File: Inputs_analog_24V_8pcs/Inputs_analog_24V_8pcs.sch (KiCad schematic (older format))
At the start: 14 parts, among them J1 Screw_Terminal_01x02, J2 Screw_Terminal_01x02, J3 Screw_Terminal_01x06, U1 SN74HC14N, U2 SN74HC14N, U3 74HC151N.652

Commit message: Update pcb
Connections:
- net GND: no longer U1.10 (5Y), U1.11 (5A), U1.12 (6Y), U1.13 (6A), U2.10 (5Y), U2.11 (5A), U2.12 (6Y), U2.13 (6A)
- net input_1: no longer U1.1 (1A)
- net input_2: no longer U1.3 (2A)
- net input_3: no longer U1.5 (3A)
- net input_4: no longer U1.9 (4A)
- net input_5: no longer U2.1 (1A)
- net input_6: no longer U2.3 (2A)
- net input_7: no longer U2.5 (3A)
- net input_8: no longer U2.9 (4A)
- net at U1.2 (1Y): no longer U3.4 (I0)
- net at U1.4 (2Y): no longer U3.3 (I1)
- net at U1.6 (3Y): no longer U3.2 (I2)
- net at U1.8 (4Y): no longer U3.1 (I3)
- net at U2.2 (1Y): no longer U3.15 (I4)
- net at U2.4 (2Y): no longer U3.14 (I5)
- net at U2.6 (3Y): no longer U3.13 (I6)
- net at U2.8 (4Y): no longer U3.12 (I7)
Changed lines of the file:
@@
 F1 "Inputs.sch" 50
 $EndSheet
-Text GLabel 1500 3900 0    50   Input ~ 0
+Text GLabel 1500 3400 0    50   Input ~ 0
 input_1
-Text GLabel 1500 3800 0    50   Input ~ 0
+Text GLabel 1500 3500 0    50   Input ~ 0
 input_2
-Text GLabel 1500 3700 0    50   Input ~ 0
+Text GLabel 1500 3600 0    50   Input ~ 0
 input_3
-Text GLabel 1500 3600 0    50   Input ~ 0
+Text GLabel 1500 3950 0    50   Input ~ 0
 input_4
+Text GLabel 1500 4750 0    50   Input ~ 0
+input_5
+Text GLabel 1500 5200 0    50   Input ~ 0
+input_6
 Text GLabel 1500 5400 0    50   Input ~ 0
-input_5
+input_7
 Text GLabel 1500 5300 0    50   Input ~ 0
-input_6
-Wire Wire Line
-	1500 3600 1950 3600
-Wire Wire Line
-	1500 3700 1950 3700
-Wire Wire Line
-	1500 3800 1950 3800
-Wire Wire Line
-	1500 3900 1950 3900
-Text GLabel 1500 5200 0    50   Input ~ 0
-input_7
-Text GLabel 1500 5100 0    50   Input ~ 0
 input_8
-Wire Wire Line
-	1500 5300 1950 5300
-Wire Wire Line
-	1500 5400 1950 5400
 $Comp
 L power:GND #PWR04
@@
 	1    0    0    -1
 $EndComp
-Wire Wire Line
-	1900 4900 1950 4900
-Wire Wire Line
-	1950 5000 1900 5000
-Connection ~ 1900 5000
-Wire Wire Line
-	1900 5000 1900 4900
 $Comp
 L power:+5V #PWR09
@@
 Wire Wire Line
 	2700 5500 2700 5700
-Connection ~ 2700 5500
-Wire Wire Line
-	2650 5000 2700 5000
-Wire Wire Line
-	2650 4900 2700 4900
-Wire Wire Line
-	2700 4900 2700 5000
-Connection ~ 2700 5000
 $Comp
 L power:+5V #PWR011
@@
 Wire Wire Line
 	4550 3900 4550 4050
-Wire Wire Line
-	1900 5000 1900 5700
-Wire Wire Line
-	1500 5200 1950 5200
-Wire Wire Line
-	1500 5100 1950 5100
 $Comp
 L power:GND #PWR03
@@
 $EndComp
 Wire Wire Line
-	1950 3500 1900 3500
-Wire Wire Line
-	1900 3500 1900 4050
-Wire Wire Line
-	1950 3400 1900 3400
-Wire Wire Line
-	1900 3400 1900 3500
-Connection ~ 1900 3500
-Wire Wire Line
-	2650 3500 2700 3500
-Wire Wire Line
-	2700 3500 2700 4000
-Connection ~ 2700 4000
-Wire Wire Line
-	2650 3400 2700 3400
-Wire Wire Line
-	2700 3400 2700 3500
-Connection ~ 2700 3500
-Wire Wire Line
-	3750 5400 3750 3500
-Wire Wire Line
-	3750 3500 3800 3500
-Wire Wire Line
-	3650 5300 3650 3400
-Wire Wire Line
-	3650 3400 3800 3400
-Wire Wire Line
-	3800 3300 3550 3300
-Wire Wire Line
-	3550 3300 3550 5200
-Wire Wire Line
-	3450 5100 3450 3200
-Wire Wire Line
-	3450 3200 3800 3200
-Wire Wire Line
-	2650 5100 3450 5100
-Wire Wire Line
-	2650 5200 3550 5200
-Wire Wire Line
-	2650 5300 3650 5300
-Wire Wire Line
-	2700 5000 2700 5500
-Wire Wire Line
-	3750 5400 2650 5400
-Wire Wire Line
-	2650 3600 3800 3600
-Wire Wire Line
-	2650 3700 3800 3700
-Wire Wire Line
-	2650 3800 3800 3800
-Wire Wire Line
-	2650 3900 3800 3900
-Wire Wire Line
 	4500 3300 4750 3300

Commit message: Update pcb
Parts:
- added R52, R53: 0, Resistor_THT:R_Axial_DIN0207_L6.3mm_D2.5mm_P7.62mm_Horizontal, symbol Device:R
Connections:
- net GND: now also U2.10 (5Y), U2.11 (5A), U2.12 (6Y), U2.13 (6A), R52.1, R53.1; no longer U1.7 (GND)
- net input_1: now also U1.13 (6A)
- net input_2: now also U1.11 (5A)
- net input_3: now also U1.9 (4A)
- net input_4: now also U2.9 (4A)
- net input_5: now also U2.5 (3A)
- net input_6: now also U2.3 (2A)
- net input_7: now also U1.1 (1A)
- net input_8: now also U2.1 (1A)
- net at U1.10 (5Y): now also U3.15 (I4)
- net at U1.12 (6Y): now also U3.14 (I5)
- net at U1.2 (1Y): now also U3.4 (I0)
- net at U1.3 (2A): now also U1.4 (2Y), U1.5 (3A), U1.6 (3Y), R52.2
- net at U1.8 (4Y): now also U3.1 (I3)
- new net: R53.2, U1.7 (GND)
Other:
- moved on the sheet: C2, U2
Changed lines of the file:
@@
 L Inputs_library:SN74HC14N U2
 U 1 1 5EA6DB6E
-P 2550 5950
-F 0 "U2" H 2300 7367 50  0000 C CNN
-F 1 "SN74HC14N" H 2300 7276 50  0000 C CNN
-F 2 "Package_DIP:DIP-14_W7.62mm" H 2550 5950 50  0001 C CNN
-F 3 "" H 2550 5950 50  0001 C CNN
-	1    2550 5950
+P 2550 6350
+F 0 "U2" H 2300 7767 50  0000 C CNN
+F 1 "SN74HC14N" H 2300 7676 50  0000 C CNN
+F 2 "Package_DIP:DIP-14_W7.62mm" H 2550 6350 50  0001 C CNN
+F 3 "" H 2550 6350 50  0001 C CNN
+	1    2550 6350
 	1    0    0    -1
 $EndComp
@@
 $EndComp
 $Sheet
-S 1000 3100 750  2700
+S 1000 3100 650  3200
 U 5EB670BF
 F0 "Inputs" 50
@@
 Text GLabel 1500 3600 0    50   Input ~ 0
 input_3
-Text GLabel 1500 3950 0    50   Input ~ 0
+Text GLabel 1500 5500 0    50   Input ~ 0
 input_4
-Text GLabel 1500 4750 0    50   Input ~ 0
+Text GLabel 1500 5600 0    50   Input ~ 0
 input_5
-Text GLabel 1500 5200 0    50   Input ~ 0
+Text GLabel 1500 5700 0    50   Input ~ 0
 input_6
-Text GLabel 1500 5400 0    50   Input ~ 0
+Text GLabel 1500 3900 0    50   Input ~ 0
 input_7
-Text GLabel 1500 5300 0    50   Input ~ 0
+Text GLabel 1500 5800 0    50   Input ~ 0
 input_8
 $Comp
 L power:GND #PWR04
 U 1 1 5EB7A823
-P 1900 5700
-F 0 "#PWR04" H 1900 5450 50  0001 C CNN
-F 1 "GND" H 1905 5527 50  0000 C CNN
-F 2 "" H 1900 5700 50  0001 C CNN
-F 3 "" H 1900 5700 50  0001 C CNN
-	1    1900 5700
+P 1900 6100
+F 0 "#PWR04" H 1900 5850 50  0001 C CNN
+F 1 "GND" H 1905 5927 50  0000 C CNN
+F 2 "" H 1900 6100 50  0001 C CNN
+F 3 "" H 1900 6100 50  0001 C CNN
+	1    1900 6100
 	1    0    0    -1
 $EndComp
@@
 L power:GND #PWR06
 U 1 1 5EBDD6D8
-P 2700 5700
-F 0 "#PWR06" H 2700 5450 50  0001 C CNN
-F 1 "GND" H 2705 5527 50  0000 C CNN
-F 2 "" H 2700 5700 50  0001 C CNN
-F 3 "" H 2700 5700 50  0001 C CNN
-	1    2700 5700
-	1    0    0    -1
-$EndComp
-Wire Wire Line
-	2650 5500 2700 5500
-Wire Wire Line
-	2700 5500 2700 5700
+P 2700 6100
+F 0 "#PWR06" H 2700 5850 50  0001 C CNN
+F 1 "GND" H 2705 5927 50  0000 C CNN
+F 2 "" H 2700 6100 50  0001 C CNN
+F 3 "" H 2700 6100 50  0001 C CNN
+	1    2700 6100
+	1    0    0    -1
+$EndComp
+Wire Wire Line
+	2650 5900 2700 5900
+Wire Wire Line
+	2700 5900 2700 6100
 $Comp
 L power:+5V #PWR011
 U 1 1 5EBE4E40
-P 3050 4800
-F 0 "#PWR011" H 3050 4650 50  0001 C CNN
-F 1 "+5V" V 3065 4928 50  0000 L CNN
-F 2 "" H 3050 4800 50  0001 C CNN
-F 3 "" H 3050 4800 50  0001 C CNN
-	1    3050 4800
-	0    1    1    0
-$EndComp
-Wire Wire Line
-	2650 4800 2700 4800
+P 3050 5200
+F 0 "#PWR011" H 3050 5050 50  0001 C CNN
+F 1 "+5V" V 3065 5328 50  0000 L CNN
+F 2 "" H 3050 5200 50  0001 C CNN
+F 3 "" H 3050 5200 50  0001 C CNN
+	1    3050 5200
+	0    1    1    0
+$EndComp
+Wire Wire Line
+	2650 5200 2700 5200
 $Comp
 L Device:C C2
 U 1 1 5EBE4E47
-P 2900 4650
-F 0 "C2" V 2648 4650 50  0000 C CNN
-F 1 "0,47μF" V 2739 4650 50  0000 C CNN
-F 2 "Capacitor_THT:C_Disc_D4.3mm_W1.9mm_P5.00mm" H 2938 4500 50  0001 C CNN
-F 3 "~" H 2900 4650 50  0001 C CNN
-	1    2900 4650
-	0    1    1    0
-$EndComp
-Wire Wire Line
-	2750 4650 2700 4650
-Wire Wire Line
-	2700 4650 2700 4800
-Connection ~ 2700 4800
+P 2900 5050
+F 0 "C2" V 2648 5050 50  0000 C CNN
+F 1 "0,47μF" V 2739 5050 50  0000 C CNN
+F 2 "Capacitor_THT:C_Disc_D4.3mm_W1.9mm_P5.00mm" H 2938 4900 50  0001 C CNN
+F 3 "~" H 2900 5050 50  0001 C CNN
+	1    2900 5050
+	0    1    1    0
+$EndComp
+Wire Wire Line
+	2750 5050 2700 5050
+Wire Wire Line
+	2700 5050 2700 5200
+Connection ~ 2700 5200
 $Comp
 L power:GND #PWR010
 U 1 1 5EBE4E50
-P 3050 4650
-F 0 "#PWR010" H 3050 4400 50  0001 C CNN
-F 1 "GND" H 3055 4477 50  0000 C CNN
-F 2 "" H 3050 4650 50  0001 C CNN
-F 3 "" H 3050 4650 50  0001 C CNN
-	1    3050 4650
+P 3050 5050
+F 0 "#PWR010" H 3050 4800 50  0001 C CNN
+F 1 "GND" H 3055 4877 50  0000 C CNN
+F 2 "" H 3050 5050 50  0001 C CNN
+F 3 "" H 3050 5050 50  0001 C CNN
+	1    3050 5050
 	0    -1   -1   0
 $EndComp
 Wire Wire Line
-	2700 4800 3050 4800
-$Comp
-L power:GND #PWR05
-U 1 1 5EBE68A6
-P 2700 4050
-F 0 "#PWR05" H 2700 3800 50  0001 C CNN
-F 1 "GND" H 2705 3877 50  0000 C CNN
-F 2 "" H 2700 4050 50  0001 C CNN
-F 3 "" H 2700 4050 50  0001 C CNN
-	1    2700 4050
-	1    0    0    -1
-$EndComp
-Wire Wire Line
-	2650 4000 2700 4000
-Wire Wire Line
-	2700 4000 2700 4050
+	2700 5200 3050 5200
 $Comp
 L power:+5V #PWR015
@@
 L power:GND #PWR03
 U 1 1 5EC164A3
-P 1900 4050
-F 0 "#PWR03" H 1900 3800 50  0001 C CNN
-F 1 "GND" H 1905 3877 50  0000 C CNN
-F 2 "" H 1900 4050 50  0001 C CNN
-F 3 "" H 1900 4050 50  0001 C CNN
-	1    1900 4050
+P 1900 4500
+F 0 "#PWR03" H 1900 4250 50  0001 C CNN
+F 1 "GND" H 1905 4327 50  0000 C CNN
+F 2 "" H 1900 4500 50  0001 C CNN
+F 3 "" H 1900 4500 50  0001 C CNN
+	1    1900 4500
 	1    0    0    -1
 $EndComp
@@
 	1    0    0    -1
 $EndComp
+Wire Wire Line
+	1500 3400 1950 3400
+Wire Wire Line
+	1500 3500 1950 3500
+Wire Wire Line
+	1500 3600 1950 3600
+Wire Wire Line
+	2650 3400 3800 3400
+Wire Wire Line
+	2650 3500 3800 3500
+Wire Wire Line
+	2650 3600 3800 3600
+Wire Wire Line
+	1500 3900 1950 3900
+Wire Wire Line
+	2650 3900 3800 3900
+$Comp
+L power:GND #PWR07
+U 1 1 5E7B992E
+P 2700 4500
+F 0 "#PWR07" H 2700 4250 50  0001 C CNN
+F 1 "GND" H 2705 4327 50  0000 C CNN
+F 2 "" H 2700 4500 50  0001 C CNN
+F 3 "" H 2700 4500 50  0001 C CNN
+	1    2700 4500
+	1    0    0    -1
+$EndComp
+$Comp
+L Device:R R52
+U 1 1 5E81BB40
+P 1900 4350
+F 0 "R52" H 1830 4304 50  0000 R CNN
+F 1 "0" H 1830 4395 50  0000 R CNN
+F 2 "Resistor_THT:R_Axial_DIN0207_L6.3mm_D2.5mm_P7.62mm_Horizontal" V 1830 4350 50  0001 C CNN
+F 3 "~" H 1900 4350 50  0001 C CNN
+	1    1900 4350
+	-1   0    0    1
+$EndComp
+$Comp
+L Device:R R53
+U 1 1 5E841327
+P 2700 4350
+F 0 "R53" H 2630 4304 50  0000 R CNN
+F 1 "0" H 2630 4395 50  0000 R CNN
+F 2 "Resistor_THT:R_Axial_DIN0207_L6.3mm_D2.5mm_P7.62mm_Horizontal" V 2630 4350 50  0001 C CNN
+F 3 "~" H 2700 4350 50  0001 C CNN
+	1    2700 4350
+	-1   0    0    1
+$EndComp
+Wire Wire Line
+	2650 4000 2700 4000
+Wire Wire Line
+	2700 4000 2700 4200
+Wire Wire Line
+	2650 3700 2800 3700
+Wire Wire Line
+	2800 3700 2800 3800
+Wire Wire Line
+	2800 4150 1900 4150
+Wire Wire Line
+	1900 4150 1900 4200
+Wire Wire Line
+	2650 3800 2800 3800
+Connection ~ 2800 3800
+Wire Wire Line
+	2800 3800 2800 4150
+Wire Wire Line
+	1950 3700 1900 3700
+Wire Wire Line
+	1900 3700 1900 3800
+Connection ~ 1900 4150
+Wire Wire Line
+	1950 3800 1900 3800
+Connection ~ 1900 3800
+Wire Wire Line
+	1900 3800 1900 4150
+Wire Wire Line
+	1500 5500 1950 5500
+Wire Wire Line
+	2650 5300 2700 5300
+Wire Wire Line
+	2700 5300 2700 5400
+Wire Wire Line
+	2700 5400 2650 5400
+Wire Wire Line
+	1950 5300 1900 5300
+Wire Wire Line
+	1900 5300 1900 5400
+Wire Wire Line
+	1900 5400 1950 5400
+Wire Wire Line
+	2700 5400 2700 5900
+Connection ~ 2700 5400
+Connection ~ 2700 5900
+Wire Wire Line
+	1900 5400 1900 6100
+Connection ~ 1900 5400
+Wire Wire Line
+	1500 5800 1950 5800
+Wire Wire Line
+	1500 5700 1950 5700
+Wire Wire Line
+	1500 5600 1950 5600
 $EndSCHEMATC

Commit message: Finish pcb
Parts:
- added R54, R55, R56, R57, R58, R59, R60, R61, R62, R63, R64, R65, R66, R67: 0, Resistor_THT:R_Axial_DIN0207_L6.3mm_D2.5mm_P7.62mm_Horizontal, symbol Device:R
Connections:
- net +5V: now also R59.1, R63.1; no longer C2.2, C3.2, U2.14 (Vcc), U3.16 (Vcc)
- net GND: now also R61.1, R64.1; no longer C2.1, C3.1, U2.7 (GND), U3.8 (GND)
- net input_5: now also R54.2; no longer U2.5 (3A)
- net input_6: now also R55.2; no longer U2.3 (2A)
- net input_8: now also R56.2; no longer U2.1 (1A)
- net at U1.10 (5Y): now also U3.2 (I2); no longer U3.15 (I4)
- net at U1.12 (6Y): now also U3.3 (I1); no longer U3.14 (I5)
- net at U2.2 (1Y): now also U3.15 (I4)
- net at U2.4 (2Y): now also U3.14 (I5)
- net at U2.6 (3Y): now also U3.13 (I6)
- net at U2.8 (4Y): now also U3.12 (I7)
- new net: R54.1, U2.5 (3A)
- new net: R55.1, U2.3 (2A)
- new net: R56.1, U2.1 (1A)
- new net: R57.1, R58.2
- new net: C3.2, R57.2, U3.16 (Vcc)
- new net: R58.1, R59.2
- new net: R60.1, R62.2
- new net: C3.1, R60.2, R61.2
- new net: R62.1, U3.8 (GND)
- new net: C2.2, R63.2, U2.14 (Vcc)
- new net: C2.1, R64.2, R66.1
- new net: R66.2, R67.1
- new net: R65.1, R67.2
- new net: R65.2, U2.7 (GND)
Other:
- moved on the sheet: C1, C2, C3, J3, R52, R53, U1, U2, U3

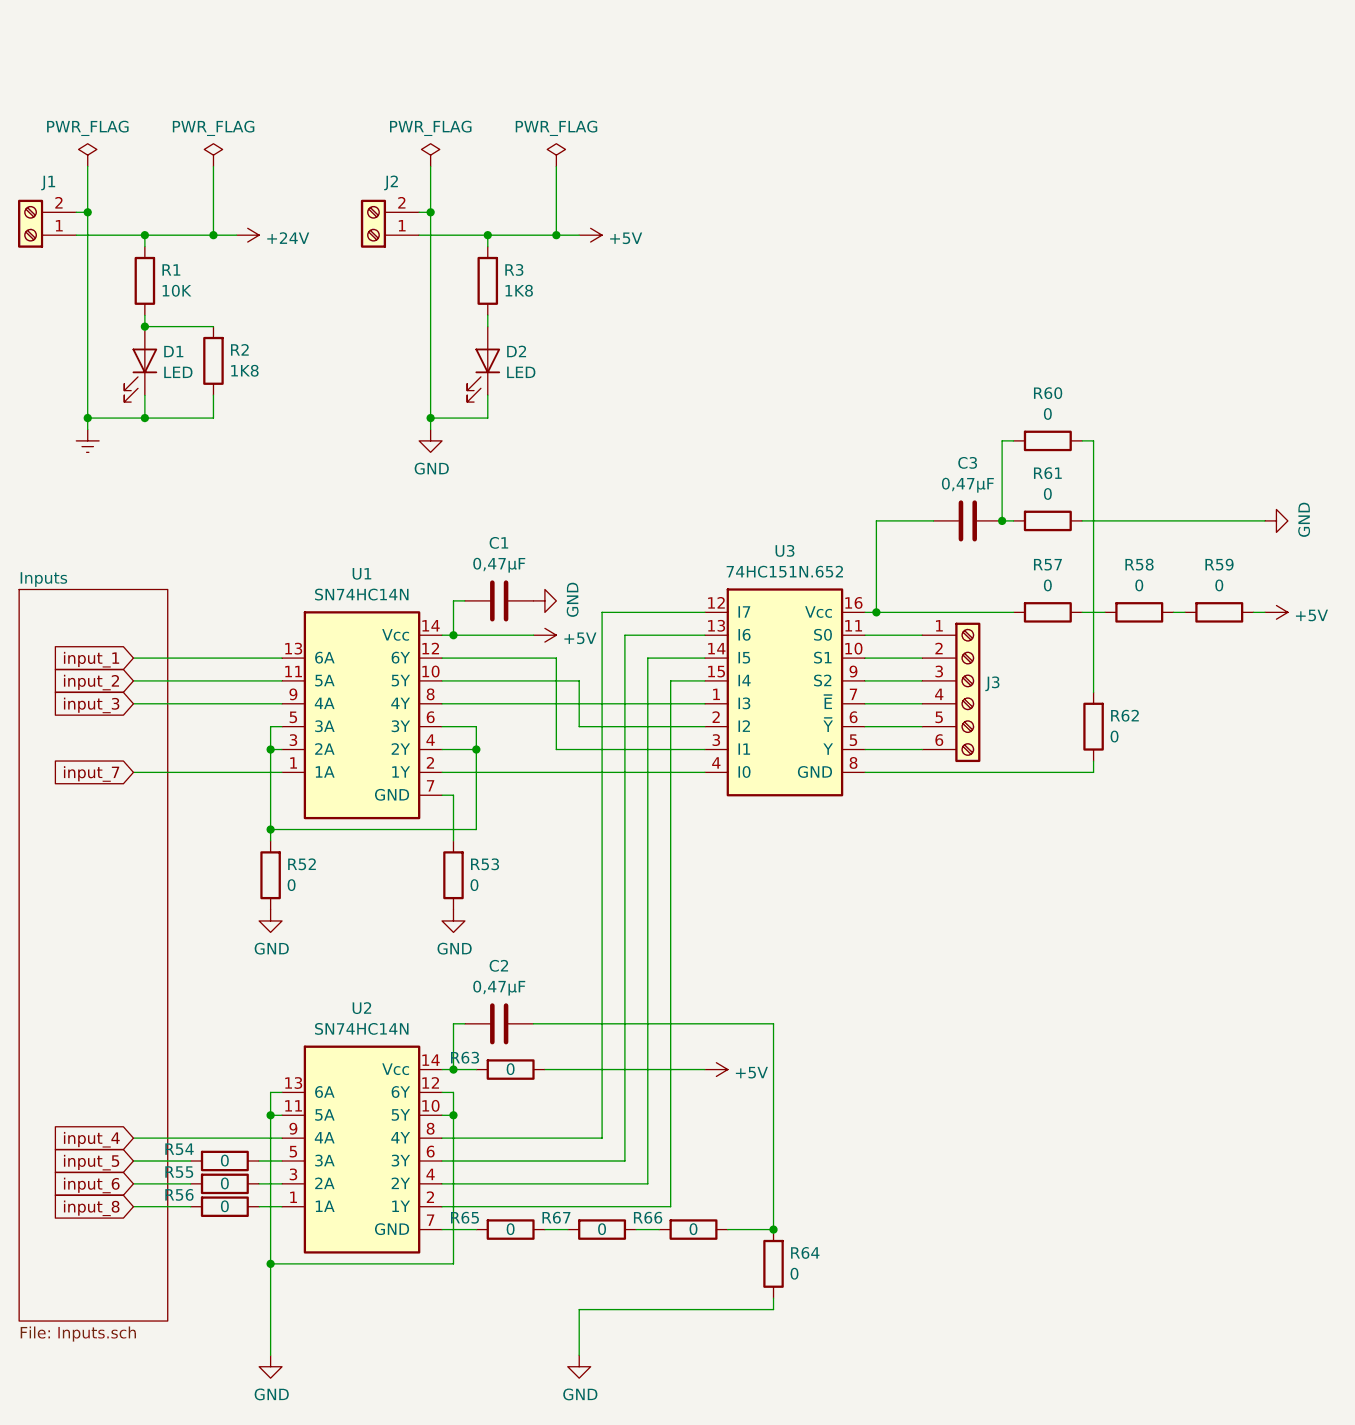
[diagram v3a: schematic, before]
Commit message: Update scmematics Add pcb second layer
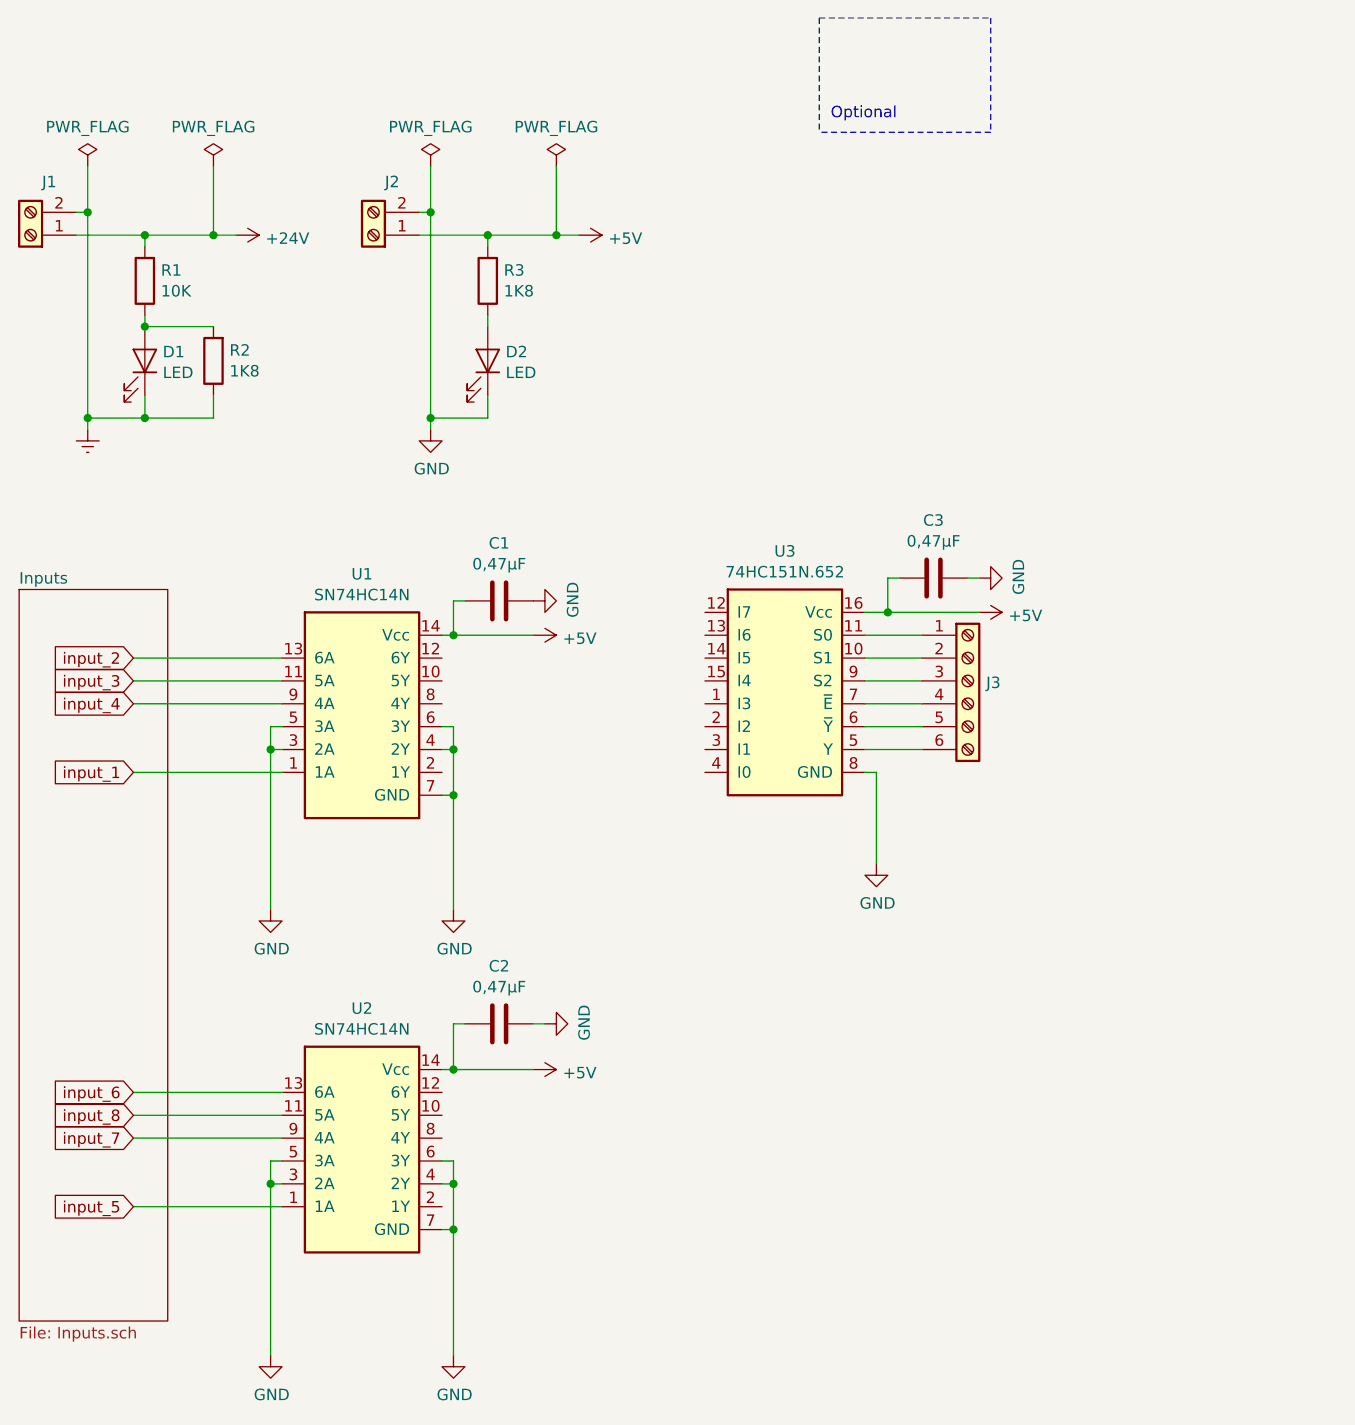
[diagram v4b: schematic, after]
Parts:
- removed R52, R53, R54, R55, R56, R57, R58, R59, R60, R61, R62, R63, R64, R65, R66, R67: 0, Resistor_THT:R_Axial_DIN0207_L6.3mm_D2.5mm_P7.62mm_Horizontal, symbol Device:R
- J1, J2: footprint Connector_PinSocket_2.54mm:PinSocket_1x02_P2.54mm_Vertical -> Connector_PinHeader_2.54mm:PinHeader_1x02_P2.54mm_Horizontal
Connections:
- net +5V: now also C2.2, C3.2, U2.14 (Vcc), U3.16 (Vcc)
- net GND: now also C2.1, C3.1, U1.3 (2A), U1.4 (2Y), U1.5 (3A), U1.6 (3Y), U1.7 (GND), U2.3 (2A), U2.4 (2Y), U2.5 (3A), U2.6 (3Y), U2.7 (GND), U3.8 (GND); no longer U2.10 (5Y), U2.11 (5A), U2.12 (6Y), U2.13 (6A)
- net input_1: now also U1.1 (1A); no longer U1.13 (6A)
- net input_2: now also U1.13 (6A); no longer U1.11 (5A)
- net input_3: now also U1.11 (5A); no longer U1.9 (4A)
- net input_4: now also U1.9 (4A); no longer U2.9 (4A)
- net input_5: now also U2.1 (1A)
- net input_6: now also U2.13 (6A)
- net input_7: now also U2.9 (4A); no longer U1.1 (1A)
- net input_8: now also U2.11 (5A)
- net at U1.10 (5Y): no longer U3.2 (I2)
- net at U1.12 (6Y): no longer U3.3 (I1)
- net at U1.2 (1Y): no longer U3.4 (I0)
- net at U1.8 (4Y): no longer U3.1 (I3)
- net at U2.2 (1Y): no longer U3.15 (I4)
- net at U3.14 (I5): no longer U2.4 (2Y)
- net at U3.13 (I6): no longer U2.6 (3Y)
- net at U2.8 (4Y): no longer U3.12 (I7)
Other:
- note added: "Optional"
- moved on the sheet: C3
